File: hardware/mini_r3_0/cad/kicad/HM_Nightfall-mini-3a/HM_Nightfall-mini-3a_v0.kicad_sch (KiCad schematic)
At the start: 97 parts, among them J2 FAN_2S3S, K1 62201021121, P1 BATTERY, Q2 SI7135DP-T1-GE3, Q3 IRLML6344TRPBF, U1 AP2210N-3.3TRG1, U2 MP6551GQB-P, U3 MP6551GQB-P, U4 ISM330DHCXTR, U5 STM32F413CHU6TRUFQFPN-48_7X7X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, U6 CY15B108QI-20LPXC, U7 MPM3610GQV-P

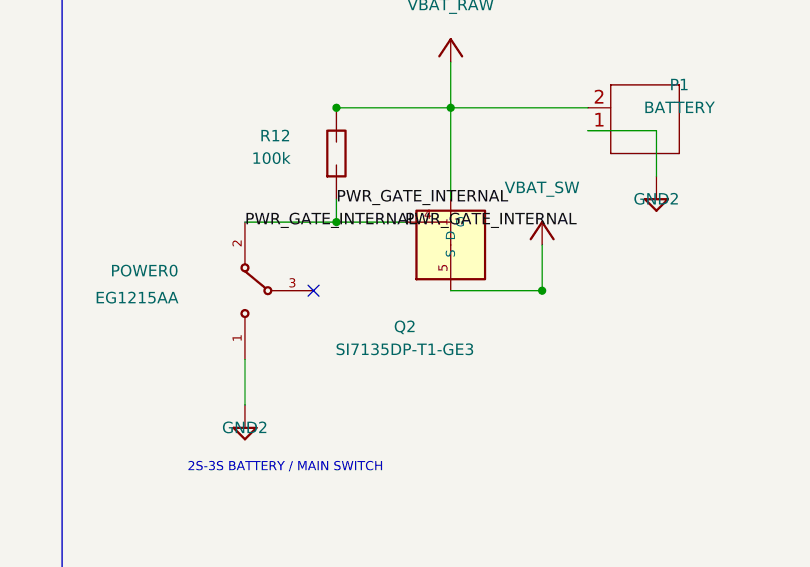
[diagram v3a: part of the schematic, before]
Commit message: Refine mini_r3 fan and control placement
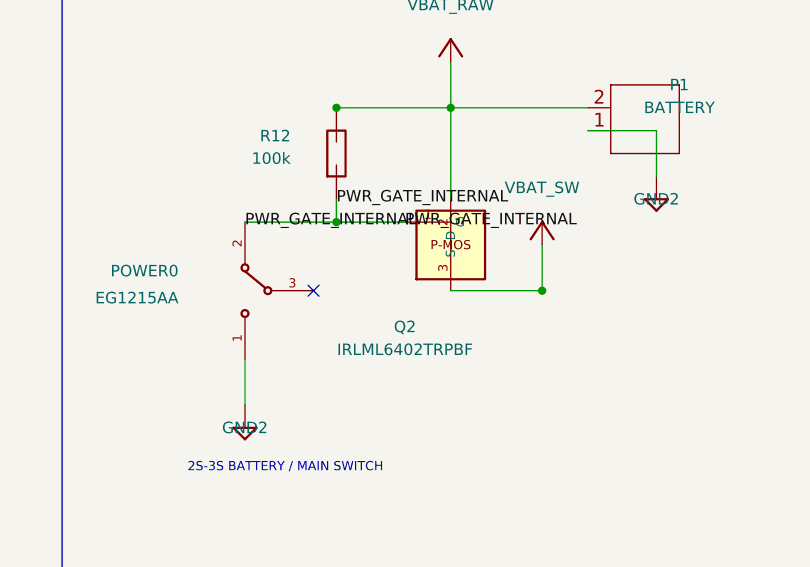
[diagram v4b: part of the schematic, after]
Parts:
- J2: footprint Connector_JST:JST_PH_B2B-PH-K_1x02_P2.00mm_Vertical -> HM_Nightfall-mini-2e_v1:FAN_WIRE_PADS_2P
- Q2: value SI7135DP-T1-GE3 -> IRLML6402TRPBF; footprint Nightfall-Power:PowerPAK_SO-8_FullPins -> Package_TO_SOT_SMD:SOT-23; symbol Nightfall-Power:SI7135DP-T1-GE3 -> Nightfall-Power:IRLML6402TRPBF
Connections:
- net PWR_GATE_INTERNAL: now also Q2.1 (G); no longer Q2.4 (G)
- net VBAT_RAW: no longer Q2.1 (S), Q2.3 (S)
- net VBAT_SW: now also Q2.3 (D); no longer Q2.5 (D), Q2.6 (D), Q2.7 (D), Q2.8 (D)
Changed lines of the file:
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@@
 			)
 		)
-		(property "Footprint" "Connector_JST:JST_PH_B2B-PH-K_1x02_P2.00mm_Vertical"
+		(property "Footprint" "HM_Nightfall-mini-2e_v1:FAN_WIRE_PADS_2P"
 			(at 431.8 101.6 0)
 			(hide yes)
@@
 	)
 	(symbol
-		(lib_id "Nightfall-Power:SI7135DP-T1-GE3")
+		(lib_id "Nightfall-Power:IRLML6402TRPBF")
 		(at 269.24 215.9 0)
 		(unit 1)
@@
 			)
 		)
-		(property "Value" "SI7135DP-T1-GE3"
+		(property "Value" "IRLML6402TRPBF"
 			(at 264.16 227.54 0)
 			(show_name no)
@@
 			)
 		)
-		(property "Footprint" "Nightfall-Power:PowerPAK_SO-8_FullPins"
+		(property "Footprint" "Package_TO_SOT_SMD:SOT-23"
 			(at 269.24 215.9 0)
 			(hide yes)
@@
 			)
 		)
-		(property "Datasheet" "https://www.vishay.com/docs/73197/si7135dp.pdf"
+		(property "Datasheet" "https://www.infineon.com/dgdl/irlml6402pbf.pdf"
 			(at 269.24 215.9 0)
 			(hide yes)
@@
 			)
 		)
-		(property "Description" ""
+		(property "Description" "P-channel MOSFET used on mini-2e; SOT-23, G=1, S=2, D=3."
 			(at 269.24 215.9 0)
 			(hide yes)
@@
 		(pin "2")
 		(pin "3")
-		(pin "4")
-		(pin "5")
-		(pin "6")
-		(pin "7")
-		(pin "8")
-		(instances
-			(project "HM_Nightfall-mini-3a_v0"
+		(instances
+			(project "HM_Nightfall-mini-3a_v0"

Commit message: Checkpoint mini_r3 four-layer routing
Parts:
- added C25: 100nF X7R, Capacitor_SMD:C_0402_1005Metric, symbol Nightfall-Power:C_VERTICAL
- added D5: BZT52-C15S_R1_00001, Diode_SMD:D_SOD-323, symbol Nightfall-Power:D_VERTICAL
- added R33: 4.7k, HM_Nightfall-mini-2e_v1:R0402, symbol Nightfall-Power:R_VERTICAL
- added R34, R35: 220k, Resistor_SMD:R_0402_1005Metric, symbol Nightfall-Power:R_VERTICAL
- C7, C9: footprint HM_Nightfall-mini-2e_v1:C0402 -> Capacitor_SMD:C_0805_2012Metric
- C_MCU-C0, C_MCU1: footprint HM_Nightfall-mini-2e_v1:C0402 -> Capacitor_SMD:C_0402_1005Metric
- D4: value BAS16WT1GW -> SM340A; footprint Package_TO_SOT_SMD:SOT-323_SC-70 -> Diode_SMD:D_SMA
- Q2: value IRLML6402TRPBF -> PJS6403_S1_00001; footprint Package_TO_SOT_SMD:SOT-23 -> Package_TO_SOT_SMD:SOT-23-6; symbol Nightfall-Power:IRLML6402TRPBF -> Nightfall-Power:PJS6403_S1_00001
- R25: footprint HM_Nightfall-mini-2e_v1:R0402 -> Resistor_SMD:R_0402_1005Metric
- U5: footprint HM_Nightfall-mini-2e_v1:UFQFPN-48_7X7X0P55MM-M -> Nightfall-Local:UFQFPN-48_7X7X0P55MM-M_noEP_hand_solder
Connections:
- net GND: now also LED2.C, LED3.C, MODE0.3, MODE0.4, R5.1, RESET0.3, RESET0.4, C25.2
- net GND2: now also R34.1, R35.1; no longer LED2.C, LED3.C, MODE0.3, MODE0.4, R5.1, RESET0.3, RESET0.4, U2.6 (SR), U3.6 (SR)
- net MOTOR_L_DIR: now also U2.5 (IN2); no longer U3.5 (IN2)
- net MOTOR_L_OUT1: now also TP3.TP, U2.1 (OUT1_2), U2.10 (OUT1); no longer TP1.TP, U3.1 (OUT1_2), U3.10 (OUT1)
- net MOTOR_L_OUT2: now also TP4.TP, U2.3 (OUT2_2), U2.8 (OUT2); no longer TP2.TP, U3.3 (OUT2_2), U3.8 (OUT2)
- net MOTOR_L_PWM: now also U2.13 (IN1); no longer U3.13 (IN1)
- net MOTOR_R_DIR: now also U3.5 (IN2); no longer U2.5 (IN2)
- net MOTOR_R_OUT1: now also TP1.TP, U3.1 (OUT1_2), U3.10 (OUT1); no longer TP3.TP, U2.1 (OUT1_2), U2.10 (OUT1)
- net MOTOR_R_OUT2: now also TP2.TP, U3.3 (OUT2_2), U3.8 (OUT2); no longer TP4.TP, U2.3 (OUT2_2), U2.8 (OUT2)
- net MOTOR_R_PWM: now also U3.13 (IN1); no longer U2.13 (IN1)
- net PWR_GATE_INTERNAL: now also Q2.3 (G), D5.1 (A), R33.1; no longer POWER0.2 (COM), Q2.1 (G)
- net VBAT_RAW: now also Q2.4 (S), D5.2 (K); no longer Q2.2 (S)
- net VBAT_SW: now also D4.2 (K), Q2.1 (D), Q2.2 (D), Q2.5 (D), Q2.6 (D); no longer D4.3 (K), Q2.3 (D)
- net VOL_CHECK: now also C25.1
- net Net-(IR_LED_R0-PadA): now reaches IR_LED_R0.A, R1R0.1
- net Net-(IR_LED_R0-C): now reaches IR_LED_R0.K (C), UR0.3 (D)
- net Net-(LED2-PadA): now reaches LED2.A, R27.1
- net Net-(LED3-PadA): now reaches LED3.A, R28.1
- net Net-(P-LED0-PadA): now reaches P-LED0.A, R25.1
- net Net-(U5B-VCAP_1): now reaches C_MCU-C0.1, U5.22 (VCAP_1)
- net Net-(U6-~{WP}): now reaches R1.2, U6.3 (~{WP})
- net Net-(IR_LED_FL0-PadA): now reaches IR_LED_FL0.A, R1FL0.1
- net Net-(IR_LED_FL0-C): now reaches IR_LED_FL0.K (C), UFL0.3 (D)
- net Net-(LED1-PadA): now reaches LED1.A, R26.1
- net Net-(D3-A): now reaches D3.1 (A), SPK1.- (+), UBUZ0.3 (D)
- net Net-(IR_LED_FR0-C): now reaches IR_LED_FR0.K (C), UFR0.3 (D)
- net Net-(IR_LED_L0-C): now reaches IR_LED_L0.K (C), UL0.3 (D)
- net Net-(IR_LED_L0-PadA): now reaches IR_LED_L0.A, R1L0.1
- net MPM_SW_INTERNAL: now reaches U7.4 (SW), U7.5 (SW), U7.6 (SW)
- net Net-(IR_LED_FR0-PadA): now reaches IR_LED_FR0.A, R1FR0.1
- new net MOTOR_L_SR: R35.2, U2.6 (SR)
- new net MOTOR_R_SR: R34.2, U3.6 (SR)
- new net PWR_SWITCH_RETURN: POWER0.2 (COM), R33.2
- no-connect marks 5 -> 17
